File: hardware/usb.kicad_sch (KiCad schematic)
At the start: 22 parts

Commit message: train schematics
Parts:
- C?: value 1u -> 4.7u; Voltage 6.3V -> 15V
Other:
- company: Erdapfel -> Frisius
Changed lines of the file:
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@@
   (title_block
     (rev "A")
-    (company "Erdapfel")
+    (company "Frisius")
   )
   (junction (at 121.92 21.59) (diameter 0) (color 0 0 0 0)
@@
       (effects (font (size 0.8 0.8)) (justify left))
     )
-    (property "Value" "1u" (id 1) (at 109.22 27.94 0)
+    (property "Value" "4.7u" (id 1) (at 109.22 27.94 0)
       (effects (font (size 0.8 0.8)) (justify left))
     )
@@
       (effects (font (size 0.8 0.8)) hide)
     )
-    (property "Voltage" "6.3V" (id 4) (at 109.22 29.21 0)
-      (effects (font (size 0.8 0.8)) (justify left))
-    )
+    (property "Voltage" "15V" (id 4) (at 109.22 29.21 0)
+      (effects (font (size 0.8 0.8)) (justify left))
+    )

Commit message: usb, charger, sensors, heir
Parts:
- added Q?: Q_NMOS_DGS, symbol Device:Q_NMOS_DGS
- added R? (x2): 10k, Resistor_SMD:R_0603_1608Metric, symbol Device:R_Small
- added R? (x3): 0, Resistor_SMD:R_0603_1608Metric, symbol Device:R_Small
- R? (x2): DNF (none) -> DNF
- R?: DNF DNF -> (none)
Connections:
- net GND: now also Q?.3 (S)
- net USB_SW: now also Q?.2 (G), R?.1, R?.2; no longer U?. (~{OE})
- net VDD_USB_3V3: now also R?.2, R?.2
- net at R?.2, U?.8 (VBUS): now also R?.2
- new net: Q?.1 (D), R?.1, R?.1, R?.1
- new net: R?.1, R?.2, U?. (~{OE})
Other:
- note added: "Another option would be to not auto switch since USB serial is only for development"
- note added: "Option: Invert USB Switch"
- note added: "USB_SW Goes low when charger power good INOKB goes low and switches to CP2102N. Invert and use this to signal USB plug in."
- moved on the sheet: C?, J?, R?, U?

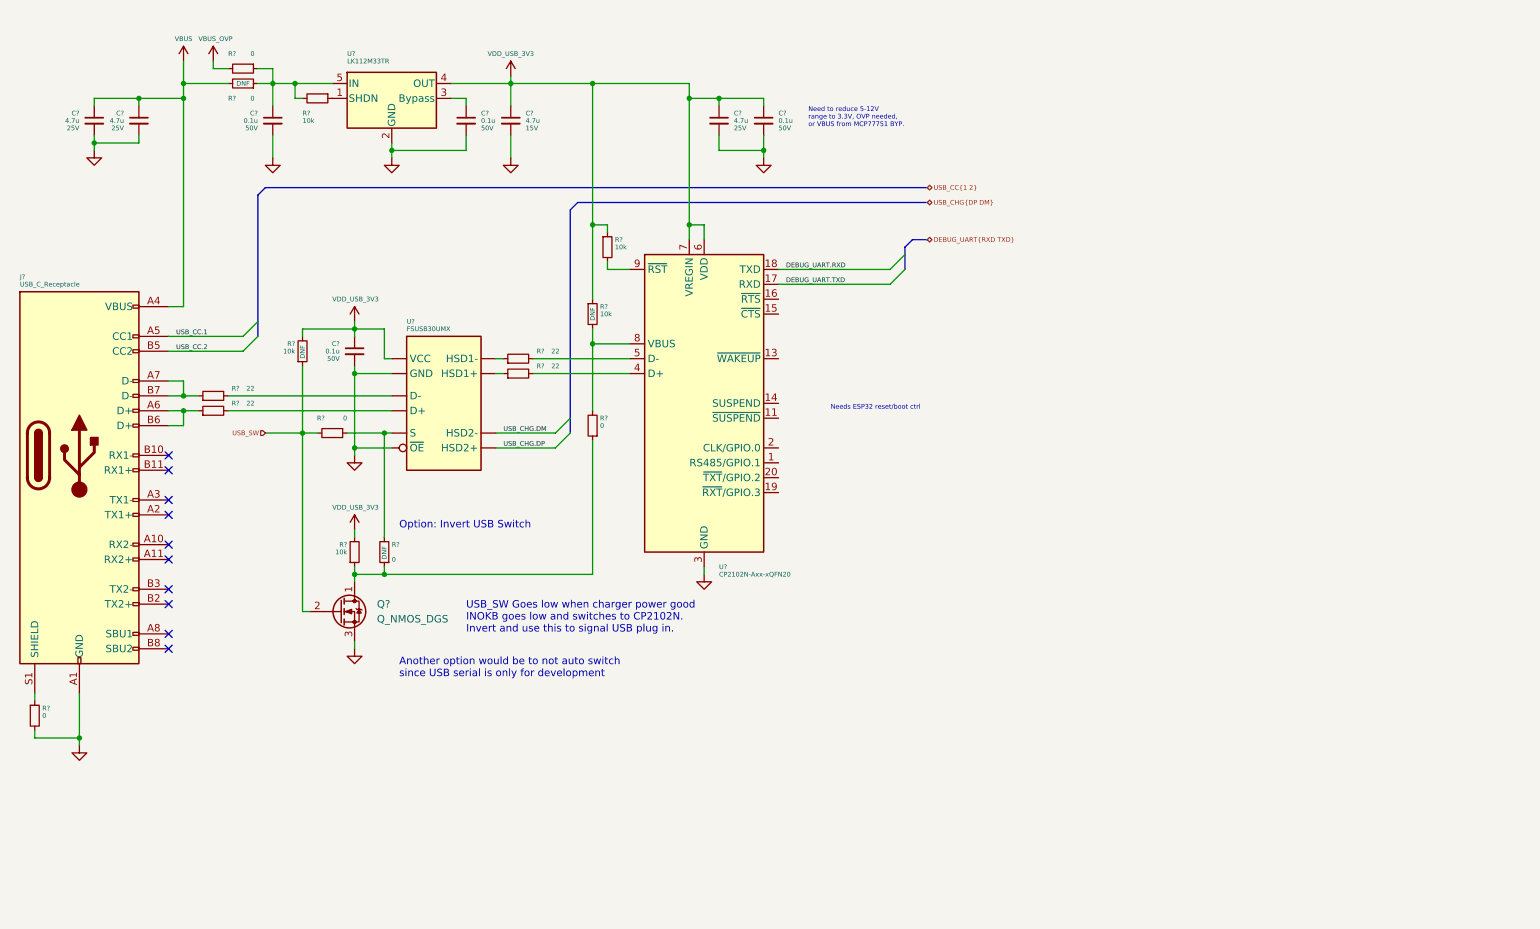
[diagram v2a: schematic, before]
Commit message: usb, bms, proc, btn changes
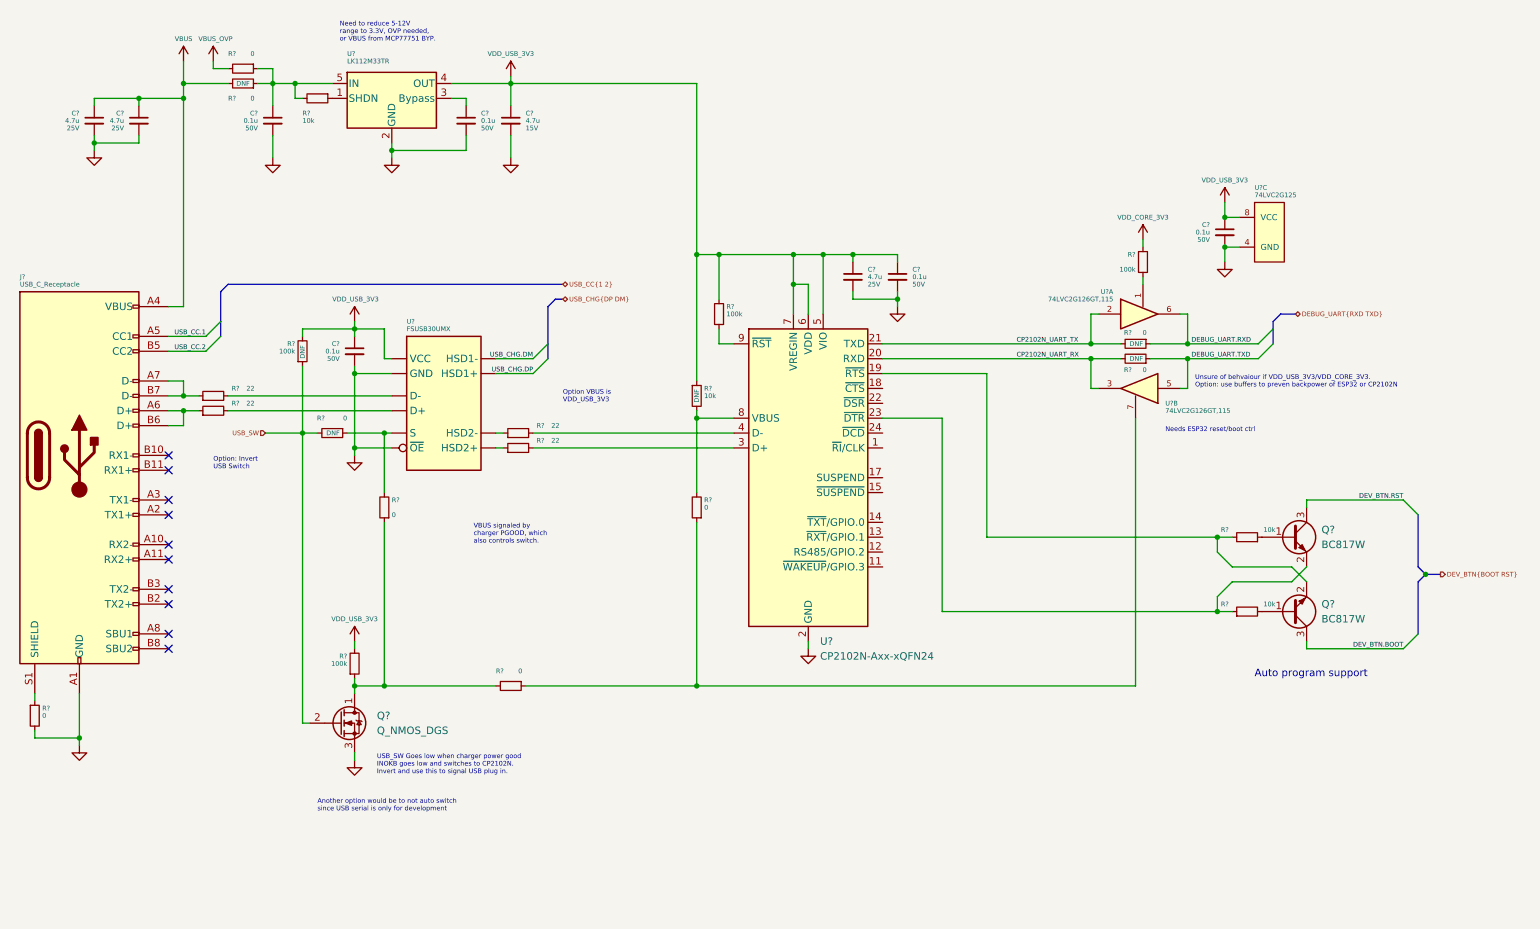
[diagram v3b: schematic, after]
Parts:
- removed U?: CP2102N-Axx-xQFN20, Package_DFN_QFN:SiliconLabs_QFN-20-1EP_3x3mm_P0.5mm, symbol Interface_USB:CP2102N-Axx-xQFN20
- added C?: 0.1u, Capacitor_SMD:C_0603_1608Metric, symbol Device:C_Small
- added Q? (x2): BC817W, Package_TO_SOT_SMD:SOT-323_SC-70, symbol Transistor_BJT:BC817W
- added R? (x3): 0, Resistor_SMD:R_0603_1608Metric, symbol Device:R_Small
- added R? (x2): 10k, Resistor_SMD:R_0603_1608Metric, symbol Device:R_Small
- added R?: 100k, Resistor_SMD:R_0603_1608Metric, symbol Device:R_Small
- added U? (x2): 74LVC2G126GT,115, symbol 74xGxx:74LVC2G125
- added U?: 74LVC2G125, symbol 74xGxx:74LVC2G125
- added U?: CP2102N-Axx-xQFN24, Package_DFN_QFN:SiliconLabs_QFN-20-1EP_3x3mm_P0.5mm_EP1.8x1.8mm, symbol Interface_USB:CP2102N-Axx-xQFN24
- R? (x3): value 10k -> 100k
- R?: DNF (none) -> DNF
- R?: DNF DNF -> (none)
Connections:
- net DEBUG_UART.RXD: now also R?.1, U?.6
- net DEBUG_UART.TXD: now also R?.1, U?.5
- net GND: now also C?.2, U?.2 (GND), U?.25 (GND), U?.4 (GND)
- net VDD_USB_3V3: now also R?.2, C?.1, U?.5 (VIO), U?.6 (VDD), U?.7 (VREGIN), U?.8 (VCC); no longer R?.1
- net at Q?.1 (D), R?.1, R?.1: now also R?.2; no longer R?.1
- net at R?.2: now also U?.3 (D+)
- net at R?.2: now also U?.4 (D-)
- net at R?.2, R?.2: now also U?.8 (VBUS)
- new net: Q?.1 (B), R?.1
- new net: Q?.2 (E), R?.2, U?.19 (~{RTS})
- new net: Q?.2 (E), R?.1, U?.23 (~{DTR})
- new net: R?.2, U?.1
- new net: Q?.1 (B), R?.2
- new net: R?.1, R?.1, U?.7
- new net: R?.1, U?.9 (~{RST})
- new net 3V3_CORE: R?.1
- new net CP2102N_UART_RX: R?.2, U?.20 (RXD), U?.3
- new net CP2102N_UART_TX: R?.2, U?.2, U?.21 (TXD)
- new net DEV_BTN.BOOT: Q?.3 (C)
- new net DEV_BTN.RST: Q?.3 (C)
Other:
- note added: "Auto program support"
- note added: "Option VBUS is VDD_USB_3V3"
- note added: "Option: use buffers to preven backpower of ESP32 or CP2102N"
- note added: "Unsure of behvaiour if VDD_USB_3V3/VDD_CORE_3V3."
- note added: "VBUS signaled by charger PGOOD, which also controls switch."
- moved on the sheet: C?, Q?, R?

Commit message: started b2b and power
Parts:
- removed C? (x2): 0.1u, Capacitor_SMD:C_0603_1608Metric, symbol Device:C_Small
- removed C?: 4.7u, Capacitor_SMD:C_0603_1608Metric, symbol Device:C_Small
- removed R? (x2): 0, Resistor_SMD:R_0603_1608Metric, symbol Device:R_Small
- removed R?: 10k, Resistor_SMD:R_0603_1608Metric, symbol Device:R_Small
- removed U?: LK112M33TR, Package_TO_SOT_SMD:SOT-23-5, symbol Regulator_Linear:LK112M33TR
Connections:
- net VBUS: no longer names the net of C?.1, C?.1, J?.A4 (VBUS), J?.A9 (VBUS), J?.B4 (VBUS), J?.B9 (VBUS)
- no-connect marks 10 -> 20
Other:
- note removed: "Need to reduce 5-12V range to 3.3V, OVP needed, or VBUS from MCP77751 BYP."
- moved on the sheet: C?, J?, Q?, R?, U?, U?A, U?B, U?C

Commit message: ready for first review
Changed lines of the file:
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@@
   (junction (at 148.59 146.05) (diameter 0) (color 0 0 0 0)
   )
-  (junction (at 212.09 90.17) (diameter 0) (color 0 0 0 0)
-  )
   (junction (at 95.25 146.05) (diameter 0) (color 0 0 0 0)
   )
@@
   )
   (junction (at 152.4 72.39) (diameter 0) (color 0 0 0 0)
-  )
-  (junction (at 212.09 87.63) (diameter 0) (color 0 0 0 0)
   )
   (junction (at 207.01 90.17) (diameter 0) (color 0 0 0 0)
@@
     (stroke (width 0) (type default) (color 0 0 0 0))
   )
-  (wire (pts (xy 212.09 90.17) (xy 215.9 90.17))
-    (stroke (width 0) (type default) (color 0 0 0 0))
-  )
   (wire (pts (xy 68.58 99.06) (xy 96.52 99.06))
     (stroke (width 0) (type default) (color 0 0 0 0))
@@
     (stroke (width 0) (type default) (color 0 0 0 0))
   )
-  (wire (pts (xy 212.09 87.63) (xy 215.9 87.63))
-    (stroke (width 0) (type default) (color 0 0 0 0))
-  )

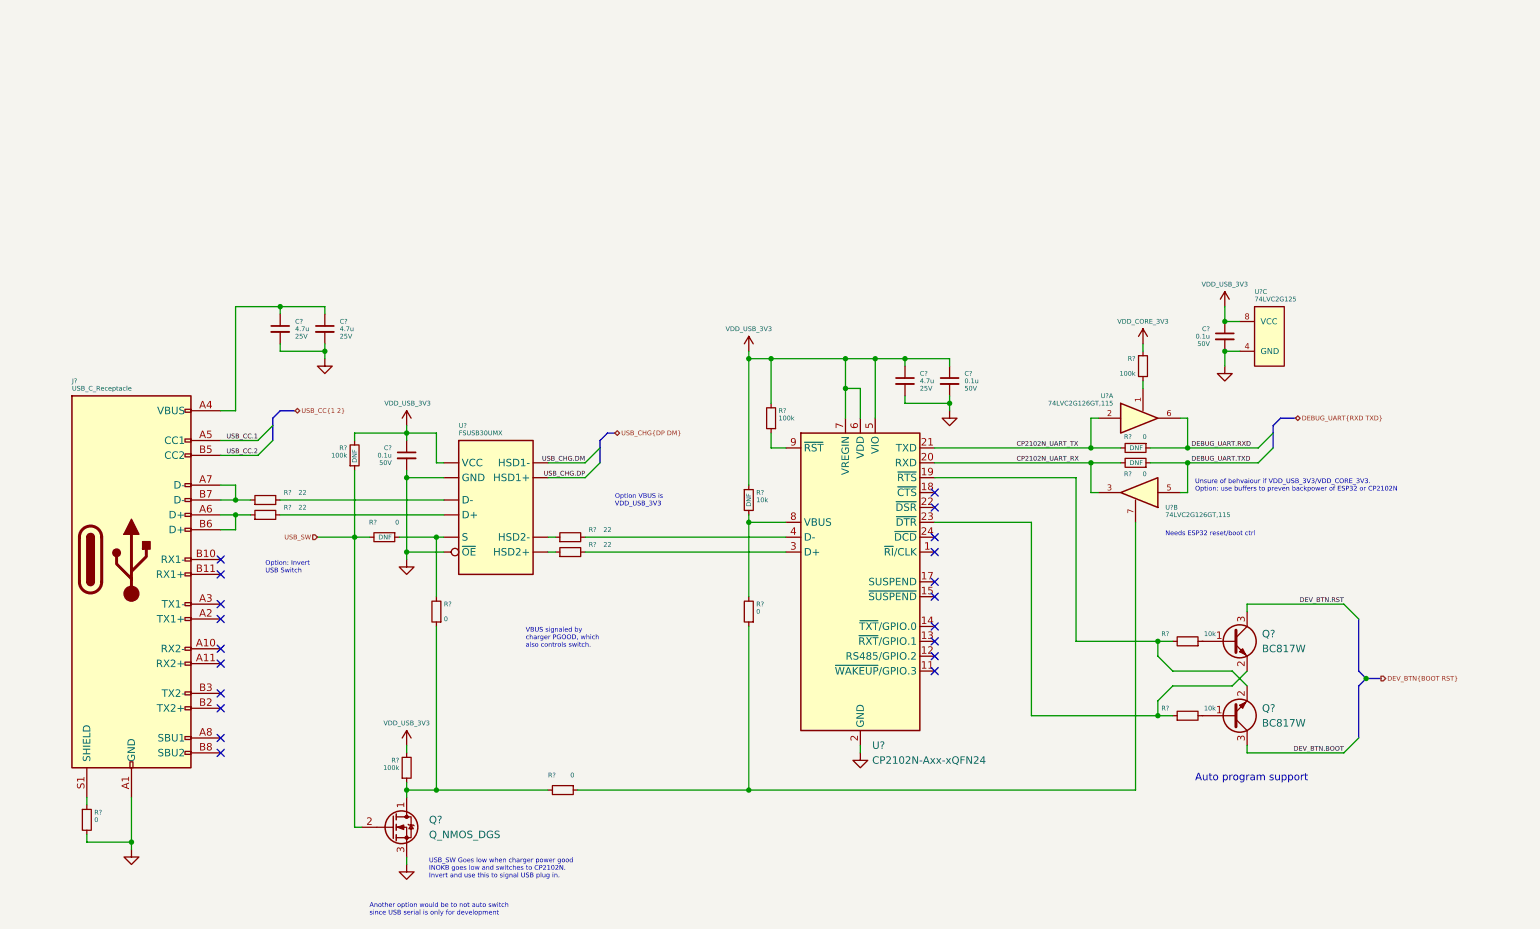
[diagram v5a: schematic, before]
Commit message: checking footprint assignment, added current sense pac1934 for dev
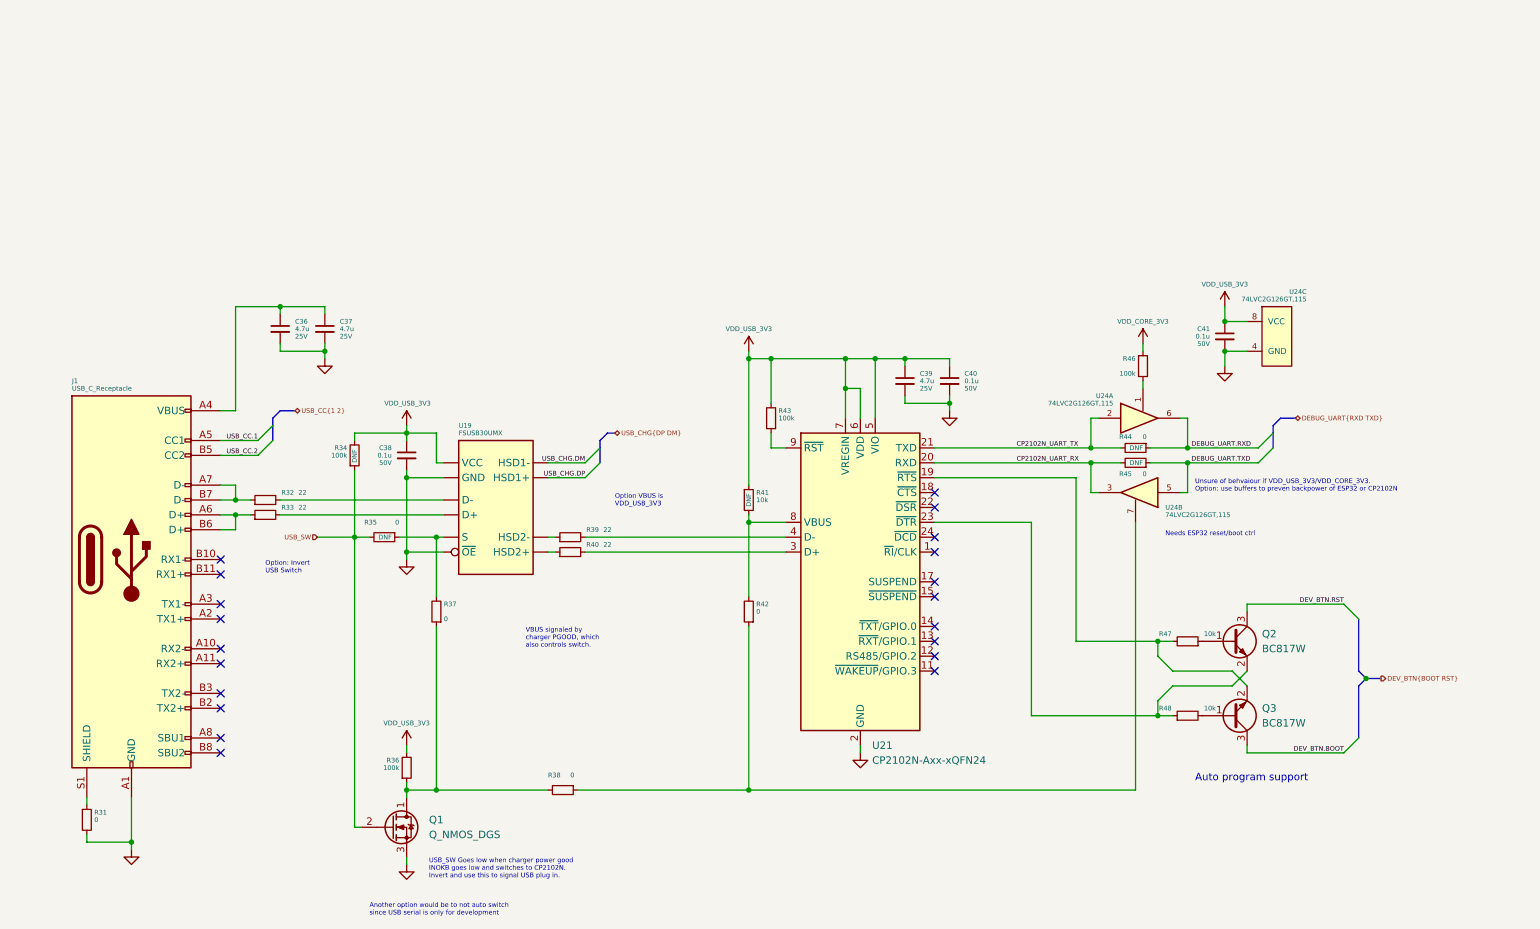
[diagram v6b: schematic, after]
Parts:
- removed U?: 74LVC2G125, symbol 74xGxx:74LVC2G125
- added unit 3 of U24
- J1: renamed from J?; footprint (none) -> bt_Connector_USB:AMPHENOL_124019032112A
- Q1: renamed from Q?; footprint (none) -> Package_TO_SOT_SMD:SOT-323_SC-70
- U19: renamed from U?; footprint Package_QFN_bt:UMLP-10-1.4x1.8_P0.4mm -> bt_Package_QFN:UMLP-10-1.4x1.8_P0.4mm
- U24: renamed from U?; footprint (none) -> Package_TO_SOT_SMD:SOT-323_SC-70
- U24: renamed from U?; value 74LVC2G126GT,115 -> 74LVC2G126GT,115; footprint (none) -> Package_TO_SOT_SMD:SOT-323_SC-70
- gave numbers to parts that had none: 27
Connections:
- net GND: now also U24.4 (GND)
- net VDD_USB_3V3: now also U24.8 (VCC)

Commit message: hardware update
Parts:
- removed Q2, Q3: BC817W, Package_TO_SOT_SMD:SOT-323_SC-70, symbol Transistor_BJT:BC817W
- removed R34, R36, R43, R46: 100k, Resistor_SMD:R_0603_1608Metric, symbol Device:R_Small
- removed R35, R37, R38, R42, R44, R45: 0, Resistor_SMD:R_0603_1608Metric, symbol Device:R_Small
- removed R39, R40: 22, Resistor_SMD:R_0603_1608Metric, symbol Device:R_Small
- removed R41, R47, R48: 10k, Resistor_SMD:R_0603_1608Metric, symbol Device:R_Small
- removed U19: FSUSB30UMX, bt_Package_QFN:UMLP-10-1.4x1.8_P0.4mm, symbol bt_IF_USB:FSUSB30UMX
- removed U21: CP2102N-Axx-xQFN24, Package_DFN_QFN:SiliconLabs_QFN-20-1EP_3x3mm_P0.5mm_EP1.8x1.8mm, symbol Interface_USB:CP2102N-Axx-xQFN24
- removed U24: 74LVC2G126GT,115, Package_TO_SOT_SMD:SOT-323_SC-70, symbol 74xGxx:74LVC2G125
- added C37: 1u, Capacitor_SMD:C_0603_1608Metric, symbol Device:C_Small
- added D4: TVS, Diode_SMD:D_SOD-523, symbol Device:D_TVS_Filled
- added D5: 3.3V, Diode_SMD:D_SOD-523, symbol Device:D_Zener_Small_Filled
- added Q2: MBT2222ADW1T1, Package_TO_SOT_SMD:SOT-363_SC-70-6, symbol Transistor_BJT:MBT2222ADW1T1
- added R23, R24, R27, R28, R29, R32, R33: 100k, Resistor_SMD:R_0402_1005Metric, symbol Device:R_Small
- added R25, R26: 22, Resistor_SMD:R_0402_1005Metric, symbol Device:R_Small
- added R30: 10k, Resistor_SMD:R_0402_1005Metric, symbol Device:R_Small
- added U10: CP2102N-Axx-xQFN24, Package_DFN_QFN:QFN-24-1EP_4x4mm_P0.5mm_EP2.6x2.6mm, symbol Interface_USB:CP2102N-Axx-xQFN24
- added U11: 74LVC2G126GT,115, Package_SON:X2SON-8_1.4x1mm_P0.35mm, symbol 74xGxx:74LVC2G125
- added U8: MAX8881EUT33+T, Package_TO_SOT_SMD:SOT-23-6, symbol bt_PMIC_Linear:MAX8881EUT33+T
- added U9: ISL54225, Package_DFN_QFN:DFN-10-1EP_3x3mm_P0.5mm_EP1.55x2.48mm, symbol bt_IF_USB:ISL54225
- C35: renamed from C36; footprint Capacitor_SMD:C_0805_2012Metric -> Capacitor_SMD:C_0603_1608Metric
- C36: renamed from C37; footprint Capacitor_SMD:C_0805_2012Metric -> Capacitor_SMD:C_0603_1608Metric
- C38, C40, C41: footprint Capacitor_SMD:C_0603_1608Metric -> Capacitor_SMD:C_0402_1005Metric
- C39: footprint Capacitor_SMD:C_0805_2012Metric -> Capacitor_SMD:C_0603_1608Metric; Voltage 25V -> 15V
- R21: renamed from R32; footprint Resistor_SMD:R_0603_1608Metric -> Resistor_SMD:R_0402_1005Metric
- R22: renamed from R33; footprint Resistor_SMD:R_0603_1608Metric -> Resistor_SMD:R_0402_1005Metric
- R31: value 0 -> 10k; footprint Resistor_SMD:R_0603_1608Metric -> Resistor_SMD:R_0402_1005Metric
- renumbered J1 to J3
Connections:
- net 3V3_CORE: now also R33.1
- net CP2102N_UART_RX: now also U10.20 (RXD), U11.3
- net CP2102N_UART_TX: now also U10.21 (TXD), U11.2
- net DEBUG_UART.RXD: now also U11.6
- net DEBUG_UART.TXD: now also U11.5
- net DEV_BTN.BOOT: now also Q2.3 (C2)
- net DEV_BTN.RST: now also Q2.6 (C1)
- net GND: now also J3.S1 (SHIELD), C37.2, D4.1 (A1), D5.2 (A), R29.2, U10.2 (GND), U10.25 (GND), U11.4 (GND), U8.2 (GND), U9.5 (GND), U9.9 (~{OE}); no longer R31.2
- net VDD_USB_3V3: now also R24.2, R27.2, R28.2, R32.2, U10.5 (VIO), U10.6 (VDD), U10.7 (VREGIN), U11.8 (VCC), U8.3 (OUT), U8.4 (FB), U9.10 (VCC)
- net at Q1.1 (D): now also R24.1, R27.1, U10.8 (VBUS), U9.1 (S)
- net VBUS: now reaches C35.1, C36.1, J3.A4 (VBUS), J3.A9 (VBUS), J3.B4 (VBUS), J3.B9 (VBUS)
- net VBUS: now also D4.2 (A2), R23.2
- net at R31.1: now also Q2.1 (E1), U10.23 (~{DTR}); no longer J3.S1 (SHIELD)
- net PORT_D+: now reaches J3.A6 (D+), J3.B6 (D+), R22.1
- net TERM_PORT_D+: now reaches R22.2
- net TERM_PORT_D+: now also U9.4 (D+)
- net PORT_D-: now reaches J3.A7 (D-), J3.B7 (D-), R21.1
- net TERM_PORT_D-: now reaches R21.2
- net TERM_PORT_D-: now also U9.6 (D-)
- new net: R33.2, U11.1
- new net: R32.1, U11.7
- new net: D5.1 (K), R23.1, U8.5 (EN)
- new net: R28.1, U10.9 (~{RST})
- new net: R29.1, U10.15 (~{SUSPEND})
- new net: Q2.4 (E2), R30.2, U10.19 (~{RTS})
- new net: Q2.5 (B2), R31.2
- new net: Q2.2 (B1), R30.1
- new net CP2102N_D+: R26.1, U9.3 (HSD2+)
- new net CP2102N_D-: R25.1, U9.2 (HSD2-)
- new net TERM_CP2102N_D+: R26.2, U10.3 (D+)
- new net TERM_CP2102N_D-: R25.2, U10.4 (D-)
- new net USB_CHG.D+: U9.8 (HSD1+)
- new net USB_CHG.D-: U9.7 (HSD1-)
- new net VDD_NVDC: C37.1, U8.1 (IN)
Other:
- note added: "Auto program support switch"
- note added: "Powers USB circuits. Control regulator with zenner regulated VBUS. Regulate VSYS for effciency."
- note removed: "Another option would be to not auto switch since USB serial is only for development"
- note removed: "Auto program support"
- note removed: "Needs ESP32 reset/boot ctrl"
- note removed: "Option VBUS is VDD_USB_3V3"
- note removed: "Option: Invert USB Switch"
- note removed: "Option: use buffers to preven backpower of ESP32 or CP2102N"
- note removed: "USB_SW Goes low when charger power good INOKB goes low and switches to CP2102N. Invert and use this to signal USB plug in."
- note removed: "Unsure of behvaiour if VDD_USB_3V3/VDD_CORE_3V3."
- note removed: "VBUS signaled by charger PGOOD, which also controls switch."
- moved on the sheet: C35, C36, C38, R21, R22
